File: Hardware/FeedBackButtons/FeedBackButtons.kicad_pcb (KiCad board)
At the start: 2 copper layers, 140 x 36 mm, 19 parts, among them SW1 SW_Push, SW2 SW_Push, SW3 SW_Push, SW4 SW_Push, U1 ESP8266-01/ESP-01, U2 AMS1117-3.3

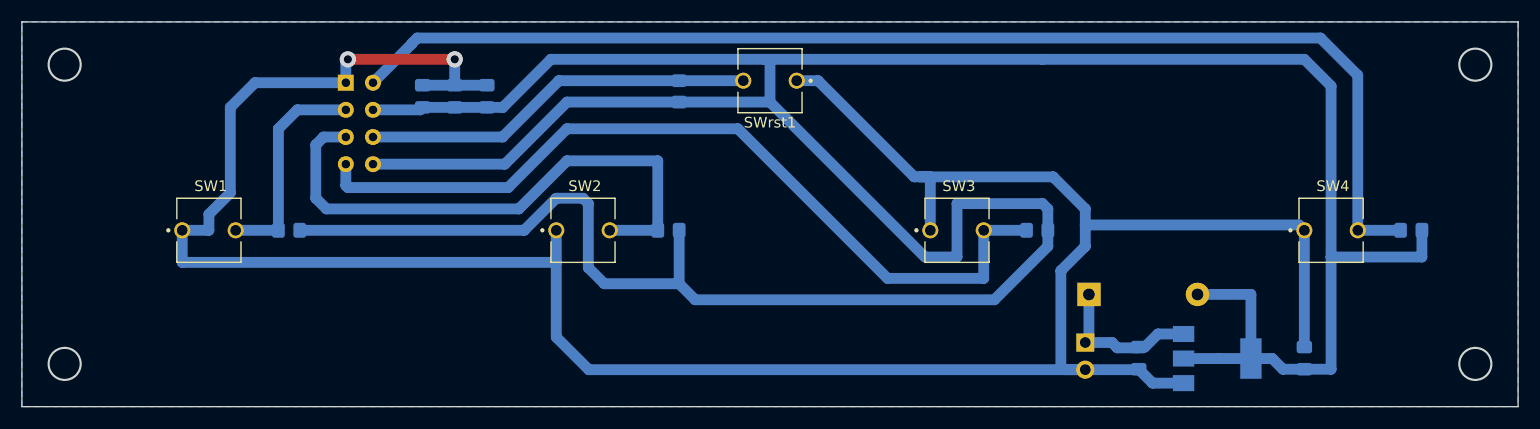
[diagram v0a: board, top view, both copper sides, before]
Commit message: Genere los Gerbers para fabricacion Demo V1
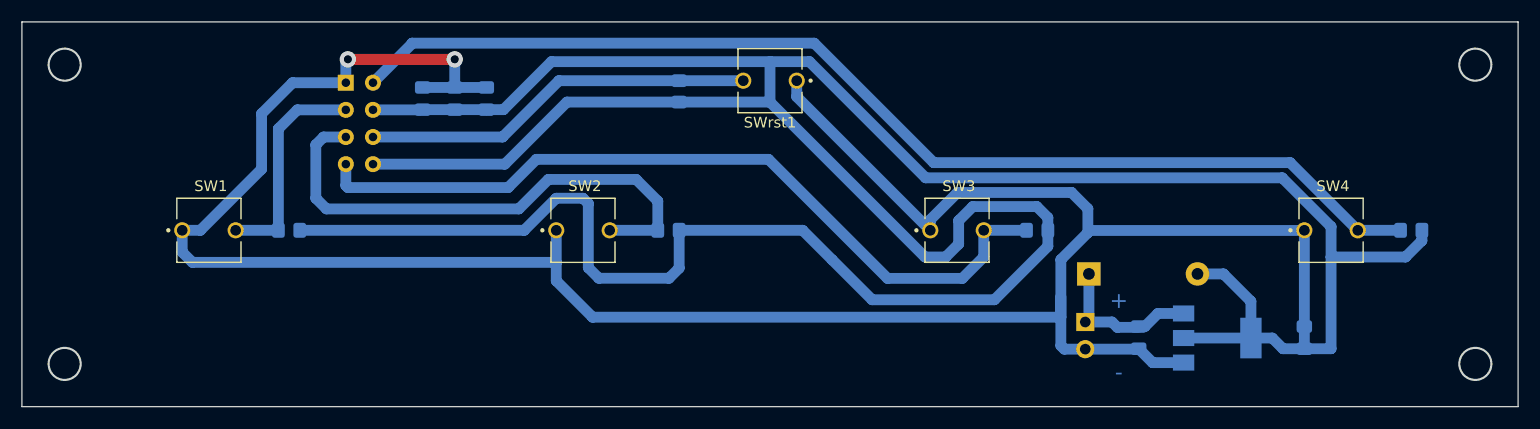
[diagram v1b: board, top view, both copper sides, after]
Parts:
- moved BT1 1.92 mm to (129.5, 127.1)
- moved C1 1.92 mm to (134.5, 128.5)
- moved C2 1.92 mm to (150.0, 128.5)
- moved D2 1.92 mm to (129.8, 122.6)
- moved U2 1.92 mm to (141.8, 128.6)
- moved C5 0.21 mm to (73.5, 106.2)
- moved C3 0.21 mm to (67.5, 106.2)
- moved C4 0.21 mm to (70.5, 106.2)
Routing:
- net +3.3V: track 325.1 -> 311.2 mm
- net GND: track 243.5 -> 230.9 mm
- net BUTTON4: track 113.9 -> 105.0 mm
- net BUTTON2: track 53.4 -> 49.7 mm
- net BUTTON3: track 78.3 -> 74.8 mm
- net +5V: track 14.6 -> 14.0 mm
- removed copper zone on B.Cu, net GND
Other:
- board text added: "+"
- board text added: "-"
